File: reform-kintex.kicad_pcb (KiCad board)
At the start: 8 copper layers, 68 x 67.8 mm, 157 parts, among them J1 Conn_01x33, U1 MNT Reform 2.0 SoM Socket, U10 W25Q128JVS, U11 TPS62823DLC, U12 TPS62823DLC, U13 TPS62823DLC, U14 TPS62823DLC, U15 TPS62823DLC, U16 TPS62823DLC, U2 XC7K160T-FFG676, U3 IS43TR16512B-125KBLI, U4 IS43TR16512B-125KBLI, U5 TPS51200DRC, U6 KSZ9031RNXCA, U7 TUSB1310ZAY, U8 TC358778XBG, U9 SiI9022A

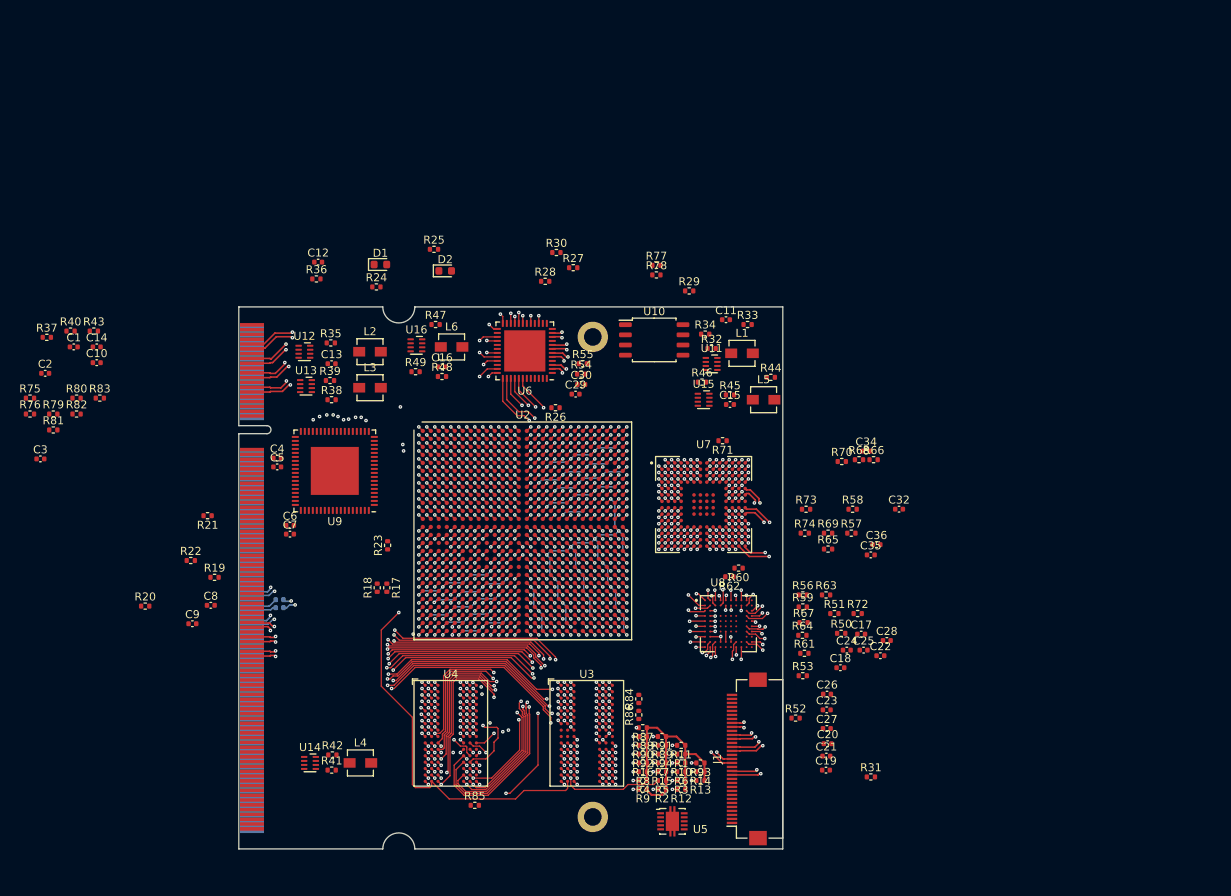
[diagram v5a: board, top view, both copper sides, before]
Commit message: more routing, bunch of fpga bypass caps, logo
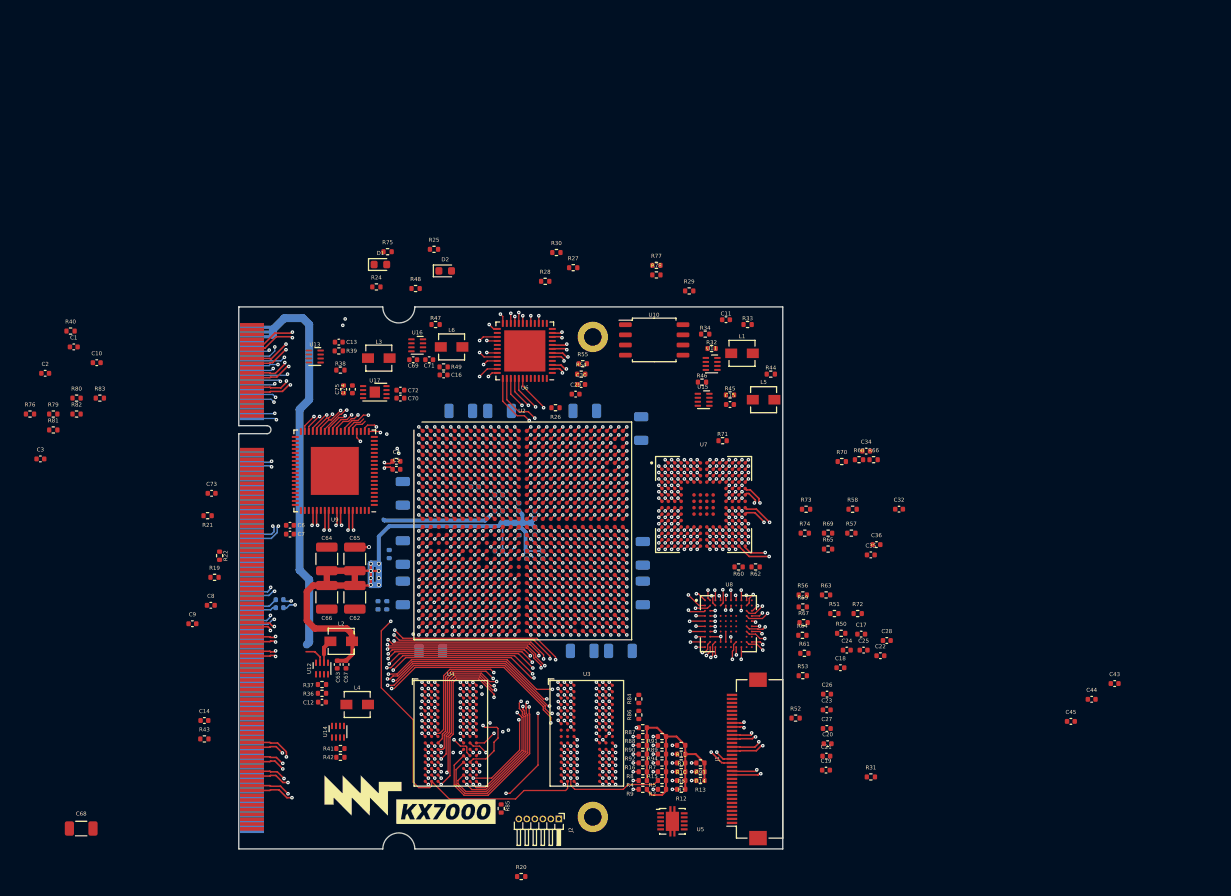
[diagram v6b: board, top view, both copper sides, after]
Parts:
- removed R35: R_Small, Resistor_SMD:R_0402_1005Metric
- added C37: 100uF, Capacitor_SMD:C_1206_3216Metric, B.Cu at (143.2, 113.0)
- added C38: 100uF, Capacitor_SMD:C_1206_3216Metric, B.Cu at (150.5, 135.8)
- added C39: 100uF, Capacitor_SMD:C_1206_3216Metric, B.Cu at (150.3, 115.2)
- added C40: 100uF, Capacitor_SMD:C_1206_3216Metric, B.Cu at (120.5, 123.3)
- added C41: 100uF, Capacitor_SMD:C_1206_3216Metric, B.Cu at (127.8, 113.0)
- added C42: 100uF, Capacitor_SMD:C_1206_3216Metric, B.Cu at (147.7, 143.0)
- added C43: 4.7uF, Capacitor_SMD:C_0402_1005Metric, F.Cu at (209.5, 147.1)
- added C44: 4.7uF, Capacitor_SMD:C_0402_1005Metric, F.Cu at (206.6, 149.1)
- added C45: 4.7uF, Capacitor_SMD:C_0402_1005Metric, F.Cu at (204.0, 151.8)
- added C46: 4.7uF, Capacitor_SMD:C_0402_1005Metric, B.Cu at (132.5, 125.5)
- added C47: 4.7uF, Capacitor_SMD:C_0402_1005Metric, B.Cu at (132.5, 123.5)
- added C48: 4.7uF, Capacitor_SMD:C_0402_1005Metric, B.Cu at (129.5, 122.5)
- added C49: 4.7uF, Capacitor_SMD:C_0402_1005Metric, B.Cu at (135.1, 128.1)
- added C50: 4.7uF, Capacitor_SMD:C_0402_1005Metric, B.Cu at (135.0, 125.0)
- added C51: 4.7uF, Capacitor_SMD:C_0402_1005Metric, B.Cu at (132.5, 130.5)
- added C52: 47uF, Capacitor_SMD:C_1206_3216Metric, B.Cu at (150.5, 130.8)
- added C53: 47uF, Capacitor_SMD:C_1206_3216Metric, B.Cu at (142.9, 143.0)
- added C54: 47uF, Capacitor_SMD:C_1206_3216Metric, B.Cu at (132.6, 113.0)
- added C55: 47uF, Capacitor_SMD:C_1206_3216Metric, B.Cu at (120.5, 130.7)
- added C56: 4.7uF, Capacitor_SMD:C_0402_1005Metric, B.Cu at (136.0, 131.0)
- added C57: 4.7uF, Capacitor_SMD:C_0402_1005Metric, B.Cu at (137.0, 128.0)
- added C58: 4.7uF, Capacitor_SMD:C_0402_1005Metric, B.Cu at (138.0, 131.0)
- added C59: 4.7uF, Capacitor_SMD:C_0402_1005Metric, B.Cu at (137.0, 126.0)
- added C60: 100uF, Capacitor_SMD:C_1206_3216Metric, B.Cu at (124.0, 143.0)
- added C61: 100uF, Capacitor_SMD:C_1206_3216Metric, B.Cu at (120.5, 135.8)
- added C62: 220uF, Capacitor_SMD:C_1210_3225Metric, F.Cu at (114.5, 136.3)
- added C63: 10uF, Capacitor_SMD:C_0402_1005Metric, F.Cu at (112.3, 144.7)
- added C64: 220uF, Capacitor_SMD:C_1210_3225Metric, F.Cu at (111.0, 131.5)
- added C65: 220uF, Capacitor_SMD:C_1210_3225Metric, F.Cu at (114.5, 131.5)
- added C66: 220uF, Capacitor_SMD:C_1210_3225Metric, F.Cu at (111.0, 136.3)
- added C67: 10uF, Capacitor_SMD:C_0402_1005Metric, F.Cu at (113.4, 144.7)
- added C68: 100uF, Capacitor_SMD:C_1206_3216Metric, F.Cu at (80.3, 165.2)
- added C69: 4.7uF, Capacitor_SMD:C_0402_1005Metric, F.Cu at (121.8, 106.6)
- added C70: 0.1uF, Capacitor_SMD:C_0402_1005Metric, F.Cu at (120.2, 111.4)
- added C71: 0.1uF, Capacitor_SMD:C_0402_1005Metric, F.Cu at (123.8, 106.6)
- added C72: 0.1uF, Capacitor_SMD:C_0402_1005Metric, F.Cu at (120.2, 110.4)
- added C73: 0.1uF, Capacitor_SMD:C_0402_1005Metric, F.Cu at (96.6, 123.3)
- added C74: 0.1uF, Capacitor_SMD:C_0402_1005Metric, F.Cu at (114.2, 110.3)
- added C75: 4.7uF, Capacitor_SMD:C_0402_1005Metric, F.Cu at (113.1, 110.3)
- added GFX1: MountingHole, footprints:mnt-kx7000, F.Cu at (121.4, 161.6)
- added J2: JTAG_01x06, Connector_PinHeader_1.00mm:PinHeader_1x06_P1.00mm_Horizontal, F.Cu at (140.0, 164.0)
- added U17: Si52112-B6, Package_DFN_QFN:TDFN-8-1EP_3x2mm_P0.5mm_EP1.3x1.4mm, F.Cu at (117.0, 110.7)
- R17, R18, R23: moved to B.Cu
- moved R20 57.9 mm to (135.3, 171.2)
- moved R37 55.4 mm to (110.4, 147.2)
- moved C12 55.0 mm to (110.4, 149.4), turned to 180 degrees
- moved R43 52.8 mm to (95.7, 154.0)
- moved R36 51.8 mm to (110.4, 148.3), turned to 180 degrees
- moved C14 48.6 mm to (95.7, 151.7)
- moved R75 48.3 mm to (118.6, 93.1)
- moved U12 39.7 mm to (110.4, 145.2), turned to 90 degrees
- moved L2 36.4 mm to (112.8, 141.8)
- moved C4 14.9 mm to (119.7, 119.3)
- moved C5 14.9 mm to (119.7, 120.3)
- moved R48 11.5 mm to (122.1, 97.7)
- moved L4 7.31 mm to (114.8, 149.7)
- moved U14 5.24 mm to (112.4, 153.1), turned to 90 degrees
- moved R39 3.86 mm to (112.5, 105.5)
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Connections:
- C12 pad 1: Net-(C12-Pad1) -> +1V0
- L2 pad 2: Net-(C12-Pad1) -> +1V0
- R36 pad 1: Net-(C12-Pad1) -> +1V0
- U12 pad 1: Net-(U12-Pad1) -> +5V
- U2 pad A8: DISP1_RGB6 -> DISP1_RGB5
- U2 pad A9: DISP1_RGB7 -> DISP1_RGB4
- U2 pad B9: DISP1_RGB4 -> DISP1_RGB6
- U2 pad C9: DISP1_RGB5 -> DISP1_RGB9
- U2 pad D10: DISP1_RGB0 -> DISP1_DE
- U2 pad D11: DISP1_VS -> DISP1_HS
- U2 pad D8: DISP1_RGB8 -> DISP1_RGB1
- U2 pad D9: DISP1_RGB9 -> DISP1_RGB10
- U2 pad E10: DISP1_RGB1 -> DISP1_RGB0
- U2 pad E11: DISP1_HS -> DISP1_VS
- U2 pad F10: DISP1_RGB2 -> DISP1_RGB7
- U2 pad F14: DISP1_DE -> DISP1_RGB11
- U2 pad F8: DISP1_RGB10 -> DISP1_RGB3
- U2 pad F9: DISP1_RGB11 -> DISP1_RGB2
- U2 pad G11: DISP1_RGB3 -> DISP1_RGB8
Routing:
- net +1V0: track 17.0 -> 106.6 mm, vias 24 -> 33
- net +5V: track 0.00 -> 57.7 mm
- net +1V8: track 93.3 -> 48.0 mm
- net HDMI_D2+: track 0.00 -> 44.6 mm, vias 0 -> 2
- net HDMI_D2-: track 0.00 -> 43.7 mm, vias 0 -> 2
- net SD2_DATA0: track 0.71 -> 43.2 mm, vias 1 -> 2
- net HDMI_D1+: track 0.00 -> 41.7 mm, vias 0 -> 2
- net HDMI_D1-: track 0.00 -> 40.9 mm, vias 0 -> 2
- net HDMI_D0+: track 0.00 -> 39.5 mm, vias 0 -> 2
- net HDMI_D0-: track 0.00 -> 38.6 mm, vias 0 -> 2
- net HDMI_CLK-: track 0.00 -> 37.9 mm, vias 0 -> 2
- net HDMI_CLK+: track 0.00 -> 36.3 mm, vias 0 -> 2
- net GND: track 161.3 -> 125.5 mm, vias 181 -> 182
- net SD2_CLK: track 0.71 -> 32.0 mm, vias 1 -> 2
- net SD2_DATA1: track 0.71 -> 29.1 mm, vias 1 -> 2
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
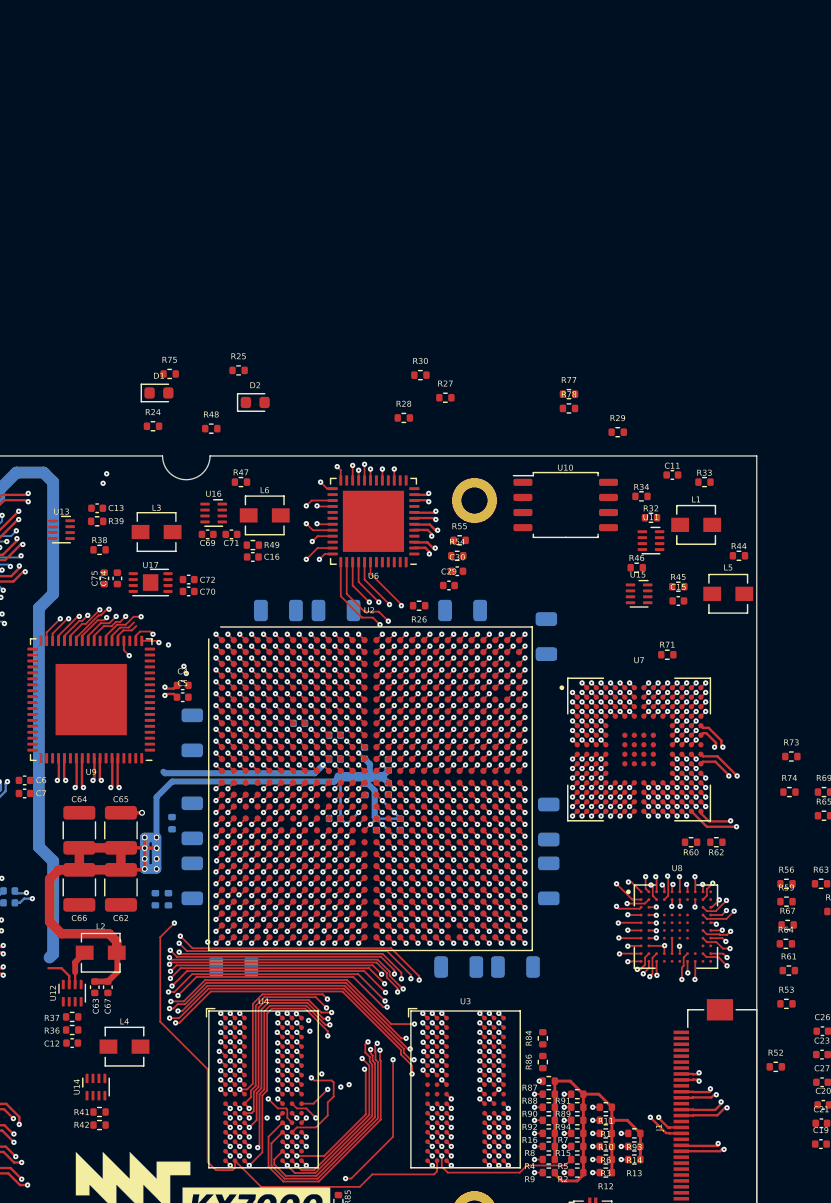
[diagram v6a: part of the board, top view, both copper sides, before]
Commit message: schematics: add many decoupling caps
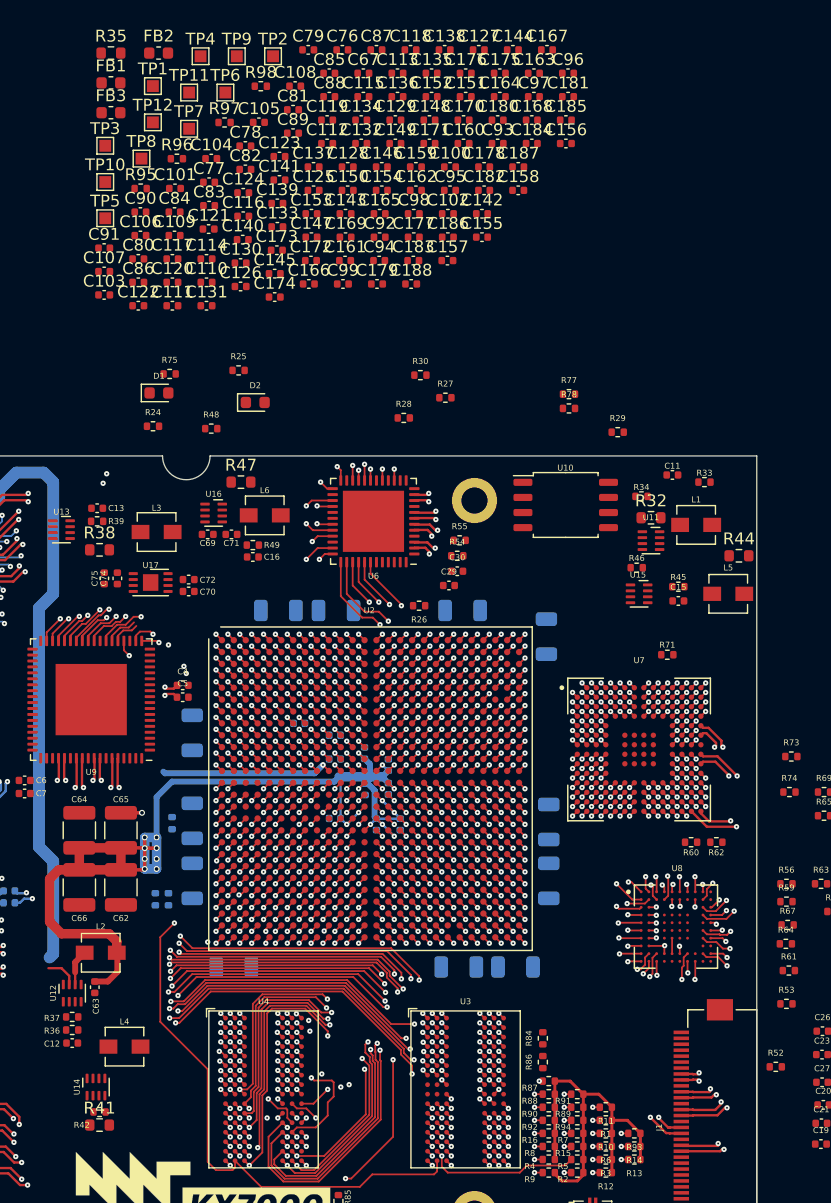
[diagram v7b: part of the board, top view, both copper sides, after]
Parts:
- added C100: 0.1uF, Capacitor_SMD:C_0402_1005Metric, F.Cu at (142.2, 75.7)
- added C101: 10uF, Capacitor_SMD:C_0402_1005Metric, F.Cu at (119.0, 77.5)
- added C102: 0.1uF, Capacitor_SMD:C_0402_1005Metric, F.Cu at (142.0, 79.6)
- added C103: 10nF, Capacitor_SMD:C_0402_1005Metric, F.Cu at (113.1, 86.5)
- added C104: 4.7uF, Capacitor_SMD:C_0402_1005Metric, F.Cu at (122.1, 75.0)
- added C105: 4.7uF, Capacitor_SMD:C_0402_1005Metric, F.Cu at (126.1, 71.9)
- added C106: 4.7uF, Capacitor_SMD:C_0402_1005Metric, F.Cu at (116.1, 81.5)
- added C107: 4.7uF, Capacitor_SMD:C_0402_1005Metric, F.Cu at (113.1, 84.5)
- added C108: 4.7uF, Capacitor_SMD:C_0402_1005Metric, F.Cu at (129.2, 68.9)
- added C109: 4.7uF, Capacitor_SMD:C_0402_1005Metric, F.Cu at (119.0, 81.5)
- added C110: 0.1uF, Capacitor_SMD:C_0402_1005Metric, F.Cu at (121.7, 85.4)
- added C111: 0.1uF, Capacitor_SMD:C_0402_1005Metric, F.Cu at (118.8, 87.4)
- added C112: 0.1uF, Capacitor_SMD:C_0402_1005Metric, F.Cu at (131.8, 73.7)
- added C113: 0.1uF, Capacitor_SMD:C_0402_1005Metric, F.Cu at (137.8, 67.8)
- added C114: 0.1uF, Capacitor_SMD:C_0402_1005Metric, F.Cu at (121.7, 83.4)
- added C115: 0.1uF, Capacitor_SMD:C_0402_1005Metric, F.Cu at (134.9, 69.8)
- added C116: 0.1uF, Capacitor_SMD:C_0402_1005Metric, F.Cu at (124.8, 79.8)
- added C117: 0.1uF, Capacitor_SMD:C_0402_1005Metric, F.Cu at (118.8, 83.4)
- added C118: 0.1uF, Capacitor_SMD:C_0402_1005Metric, F.Cu at (138.9, 65.8)
- added C119: 0.1uF, Capacitor_SMD:C_0402_1005Metric, F.Cu at (131.8, 71.7)
- added C120: 0.1uF, Capacitor_SMD:C_0402_1005Metric, F.Cu at (118.8, 85.4)
- added C121: 0.1uF, Capacitor_SMD:C_0402_1005Metric, F.Cu at (121.9, 80.9)
- added C122: 0.1uF, Capacitor_SMD:C_0402_1005Metric, F.Cu at (116.0, 87.4)
- added C123: 0.1uF, Capacitor_SMD:C_0402_1005Metric, F.Cu at (127.8, 74.8)
- added C124: 0.1uF, Capacitor_SMD:C_0402_1005Metric, F.Cu at (124.8, 77.9)
- added C125: 0.1uF, Capacitor_SMD:C_0402_1005Metric, F.Cu at (130.7, 77.7)
- added C126: 0.1uF, Capacitor_SMD:C_0402_1005Metric, F.Cu at (124.6, 85.7)
- added C127: 0.1uF, Capacitor_SMD:C_0402_1005Metric, F.Cu at (144.6, 65.8)
- added C128: 0.1uF, Capacitor_SMD:C_0402_1005Metric, F.Cu at (133.6, 75.7)
- added C129: 0.1uF, Capacitor_SMD:C_0402_1005Metric, F.Cu at (137.6, 71.7)
- added C130: 0.1uF, Capacitor_SMD:C_0402_1005Metric, F.Cu at (124.6, 83.8)
- added C131: 0.1uF, Capacitor_SMD:C_0402_1005Metric, F.Cu at (121.7, 87.4)
- added C132: 0.1uF, Capacitor_SMD:C_0402_1005Metric, F.Cu at (134.7, 73.7)
- added C133: 0.1uF, Capacitor_SMD:C_0402_1005Metric, F.Cu at (127.7, 80.7)
- added C134: 0.1uF, Capacitor_SMD:C_0402_1005Metric, F.Cu at (134.7, 71.7)
- added C135: 0.1uF, Capacitor_SMD:C_0402_1005Metric, F.Cu at (140.6, 67.8)
- added C136: 0.1uF, Capacitor_SMD:C_0402_1005Metric, F.Cu at (137.8, 69.8)
- added C137: 0.1uF, Capacitor_SMD:C_0402_1005Metric, F.Cu at (130.7, 75.7)
- added C138: 0.1uF, Capacitor_SMD:C_0402_1005Metric, F.Cu at (141.7, 65.8)
- added C139: 0.1uF, Capacitor_SMD:C_0402_1005Metric, F.Cu at (127.7, 78.8)
- added C140: 0.1uF, Capacitor_SMD:C_0402_1005Metric, F.Cu at (124.8, 81.8)
- added C141: 0.1uF, Capacitor_SMD:C_0402_1005Metric, F.Cu at (127.8, 76.8)
- added C142: 0.1uF, Capacitor_SMD:C_0402_1005Metric, F.Cu at (144.9, 79.6)
- added C143: 0.1uF, Capacitor_SMD:C_0402_1005Metric, F.Cu at (133.4, 79.6)
- added C144: 0.1uF, Capacitor_SMD:C_0402_1005Metric, F.Cu at (147.5, 65.8)
- added C145: 0.1uF, Capacitor_SMD:C_0402_1005Metric, F.Cu at (127.4, 84.7)
- added C146: 0.1uF, Capacitor_SMD:C_0402_1005Metric, F.Cu at (136.4, 75.7)
- added C147: 0.1uF, Capacitor_SMD:C_0402_1005Metric, F.Cu at (130.5, 81.6)
- added C148: 0.1uF, Capacitor_SMD:C_0402_1005Metric, F.Cu at (140.5, 71.7)
- added C149: 0.1uF, Capacitor_SMD:C_0402_1005Metric, F.Cu at (137.6, 73.7)
- added C150: 0.1uF, Capacitor_SMD:C_0402_1005Metric, F.Cu at (133.6, 77.7)
- added C151: 0.1uF, Capacitor_SMD:C_0402_1005Metric, F.Cu at (143.5, 69.8)
- added C152: 0.1uF, Capacitor_SMD:C_0402_1005Metric, F.Cu at (140.6, 69.8)
- added C153: 0.1uF, Capacitor_SMD:C_0402_1005Metric, F.Cu at (130.5, 79.6)
- added C154: 0.1uF, Capacitor_SMD:C_0402_1005Metric, F.Cu at (136.4, 77.7)
- added C155: 0.1uF, Capacitor_SMD:C_0402_1005Metric, F.Cu at (144.9, 81.6)
- added C156: 0.1uF, Capacitor_SMD:C_0402_1005Metric, F.Cu at (151.9, 73.7)
- added C157: 0.1uF, Capacitor_SMD:C_0402_1005Metric, F.Cu at (142.0, 83.6)
- added C158: 0.1uF, Capacitor_SMD:C_0402_1005Metric, F.Cu at (147.9, 77.7)
- added C159: 0.1uF, Capacitor_SMD:C_0402_1005Metric, F.Cu at (139.3, 75.7)
- added C160: 0.1uF, Capacitor_SMD:C_0402_1005Metric, F.Cu at (143.3, 73.7)
- added C161: 0.1uF, Capacitor_SMD:C_0402_1005Metric, F.Cu at (133.4, 83.6)
- added C162: 0.1uF, Capacitor_SMD:C_0402_1005Metric, F.Cu at (139.3, 77.7)
- added C163: 0.1uF, Capacitor_SMD:C_0402_1005Metric, F.Cu at (149.2, 67.8)
- added C164: 0.1uF, Capacitor_SMD:C_0402_1005Metric, F.Cu at (146.4, 69.8)
- added C165: 0.1uF, Capacitor_SMD:C_0402_1005Metric, F.Cu at (136.3, 79.6)
- added C166: 1uF, Capacitor_SMD:C_0402_1005Metric, F.Cu at (130.3, 85.5)
- added C167: 0.1uF, Capacitor_SMD:C_0402_1005Metric, F.Cu at (150.3, 65.8)
- added C168: 0.1uF, Capacitor_SMD:C_0402_1005Metric, F.Cu at (149.1, 71.7)
- added C169: 0.1uF, Capacitor_SMD:C_0402_1005Metric, F.Cu at (133.4, 81.6)
- added C170: 0.1uF, Capacitor_SMD:C_0402_1005Metric, F.Cu at (143.3, 71.7)
- added C171: 0.1uF, Capacitor_SMD:C_0402_1005Metric, F.Cu at (140.5, 73.7)
- added C172: 0.1uF, Capacitor_SMD:C_0402_1005Metric, F.Cu at (130.5, 83.6)
- added C173: 0.1uF, Capacitor_SMD:C_0402_1005Metric, F.Cu at (127.6, 82.7)
- added C174: 0.1uF, Capacitor_SMD:C_0402_1005Metric, F.Cu at (127.4, 86.6)
- added C175: 0.1uF, Capacitor_SMD:C_0402_1005Metric, F.Cu at (146.4, 67.8)
- added C176: 0.1uF, Capacitor_SMD:C_0402_1005Metric, F.Cu at (143.5, 67.8)
- added C177: 0.1uF, Capacitor_SMD:C_0402_1005Metric, F.Cu at (139.1, 81.6)
- added C178: 0.1uF, Capacitor_SMD:C_0402_1005Metric, F.Cu at (145.1, 75.7)
- added C179: 1uF, Capacitor_SMD:C_0402_1005Metric, F.Cu at (136.1, 85.5)
- added C180: 0.1uF, Capacitor_SMD:C_0402_1005Metric, F.Cu at (146.2, 71.7)
- added C181: 0.1uF, Capacitor_SMD:C_0402_1005Metric, F.Cu at (152.1, 69.8)
- added C182: 0.1uF, Capacitor_SMD:C_0402_1005Metric, F.Cu at (145.1, 77.7)
- added C183: 0.1uF, Capacitor_SMD:C_0402_1005Metric, F.Cu at (139.1, 83.6)
- added C184: 0.1uF, Capacitor_SMD:C_0402_1005Metric, F.Cu at (149.1, 73.7)
- added C185: 0.1uF, Capacitor_SMD:C_0402_1005Metric, F.Cu at (151.9, 71.7)
- added C186: 0.1uF, Capacitor_SMD:C_0402_1005Metric, F.Cu at (142.0, 81.6)
- added C187: 1uF, Capacitor_SMD:C_0402_1005Metric, F.Cu at (147.9, 75.7)
- added C188: 0.1uF, Capacitor_SMD:C_0402_1005Metric, F.Cu at (138.9, 85.5)
- added C76: 10uF, Capacitor_SMD:C_0402_1005Metric, F.Cu at (133.1, 65.8)
- added C77: 10uF, Capacitor_SMD:C_0402_1005Metric, F.Cu at (121.9, 77.0)
- added C78: 4.7uF, Capacitor_SMD:C_0402_1005Metric, F.Cu at (125.0, 73.9)
- added C79: 10uF, Capacitor_SMD:C_0402_1005Metric, F.Cu at (130.3, 65.8)
- added C80: 10uF, Capacitor_SMD:C_0402_1005Metric, F.Cu at (116.0, 83.4)
- added C81: 10uF, Capacitor_SMD:C_0402_1005Metric, F.Cu at (129.0, 70.9)
- added C82: 10uF, Capacitor_SMD:C_0402_1005Metric, F.Cu at (125.0, 75.9)
- added C83: 0.1uF, Capacitor_SMD:C_0402_1005Metric, F.Cu at (121.9, 78.9)
- added C84: 0.1uF, Capacitor_SMD:C_0402_1005Metric, F.Cu at (119.0, 79.5)
- added C85: 0.1uF, Capacitor_SMD:C_0402_1005Metric, F.Cu at (132.0, 67.8)
- added C86: 0.1uF, Capacitor_SMD:C_0402_1005Metric, F.Cu at (116.0, 85.4)
- added C87: 0.1uF, Capacitor_SMD:C_0402_1005Metric, F.Cu at (136.0, 65.8)
- added C88: 0.1uF, Capacitor_SMD:C_0402_1005Metric, F.Cu at (132.0, 69.8)
- added C89: 10uF, Capacitor_SMD:C_0402_1005Metric, F.Cu at (129.0, 72.8)
- added C90: 0.1uF, Capacitor_SMD:C_0402_1005Metric, F.Cu at (116.1, 79.5)
- added C91: 0.1uF, Capacitor_SMD:C_0402_1005Metric, F.Cu at (113.1, 82.5)
- added C92: 0.1uF, Capacitor_SMD:C_0402_1005Metric, F.Cu at (136.3, 81.6)
- added C93: 10uF, Capacitor_SMD:C_0402_1005Metric, F.Cu at (146.2, 73.7)
- added C94: 10uF, Capacitor_SMD:C_0402_1005Metric, F.Cu at (136.2, 83.6)
- added C95: 0.1uF, Capacitor_SMD:C_0402_1005Metric, F.Cu at (142.2, 77.7)
- added C96: 0.1uF, Capacitor_SMD:C_0402_1005Metric, F.Cu at (152.1, 67.8)
- added C97: 10uF, Capacitor_SMD:C_0402_1005Metric, F.Cu at (149.2, 69.8)
- added C98: 10uF, Capacitor_SMD:C_0402_1005Metric, F.Cu at (139.1, 79.6)
- added C99: 0.1uF, Capacitor_SMD:C_0402_1005Metric, F.Cu at (133.2, 85.5)
- added FB1: Ferrite_Bead_Small, Inductor_SMD:L_0603_1608Metric, F.Cu at (113.7, 68.6)
- added FB2: Ferrite_Bead_Small, Inductor_SMD:L_0603_1608Metric, F.Cu at (117.7, 66.1)
- added FB3: Ferrite_Bead_Small, Inductor_SMD:L_0603_1608Metric, F.Cu at (113.7, 71.1)
- added R35: 0, Resistor_SMD:R_0603_1608Metric, F.Cu at (113.7, 66.1)
- added R95: 4.7k, Resistor_SMD:R_0402_1005Metric, F.Cu at (116.2, 77.5)
- added R96: 5.1k, Resistor_SMD:R_0402_1005Metric, F.Cu at (119.2, 75.0)
- added R97: 10k, Resistor_SMD:R_0402_1005Metric, F.Cu at (123.2, 71.9)
- added R98: 100, Resistor_SMD:R_0402_1005Metric, F.Cu at (126.3, 68.9)
- added TP1: TestPoint, TestPoint:TestPoint_Pad_1.0x1.0mm, F.Cu at (117.2, 68.9)
- added TP10: TUSBJ_TDI, TestPoint:TestPoint_Pad_1.0x1.0mm, F.Cu at (113.2, 77.0)
- added TP11: TUSBJ_TRSTN, TestPoint:TestPoint_Pad_1.0x1.0mm, F.Cu at (120.2, 69.4)
- added TP12: TUSBJ_TDO, TestPoint:TestPoint_Pad_1.0x1.0mm, F.Cu at (117.2, 71.9)
- added TP2: TestPoint, TestPoint:TestPoint_Pad_1.0x1.0mm, F.Cu at (127.3, 66.4)
- added TP3: TestPoint, TestPoint:TestPoint_Pad_1.0x1.0mm, F.Cu at (113.2, 73.9)
- added TP4: TestPoint, TestPoint:TestPoint_Pad_1.0x1.0mm, F.Cu at (121.2, 66.4)
- added TP5: TestPoint, TestPoint:TestPoint_Pad_1.0x1.0mm, F.Cu at (113.2, 80.0)
- added TP6: TestPoint, TestPoint:TestPoint_Pad_1.0x1.0mm, F.Cu at (123.3, 69.4)
- added TP7: TestPoint, TestPoint:TestPoint_Pad_1.0x1.0mm, F.Cu at (120.2, 72.5)
- added TP8: TUSBJ_TCK, TestPoint:TestPoint_Pad_1.0x1.0mm, F.Cu at (116.2, 75.0)
- added TP9: TUSBJ_TMS, TestPoint:TestPoint_Pad_1.0x1.0mm, F.Cu at (124.2, 66.4)
- C67: value 10uF -> 4.7uF
- R32, R38, R41, R44, R47: value R_Small -> 0; footprint Resistor_SMD:R_0402_1005Metric -> Resistor_SMD:R_0603_1608Metric
- moved C67 79.8 mm to (134.9, 67.8), turned to 0 degrees
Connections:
- net Net-(U9-Pad1) renamed DISP1_SCL
- net Net-(U9-Pad2) renamed DISP1_SDA
- C12 pad 1: +1V0 -> Net-(C12-Pad1)
- C63 pad 1: +1V0 -> Net-(C12-Pad1)
- C67 pad 1: +1V0 -> GND
- C67 pad 2: GND -> +5V
- L2 pad 2: +1V0 -> Net-(C12-Pad1)
- R36 pad 1: +1V0 -> Net-(C12-Pad1)
- U12 pad 1: +5V -> Net-(U12-Pad1)
- U2 pad M5: Net-(U2-PadM5) -> +1V2
- U6 pad 1: Net-(U6-Pad1) -> ETH_VDDA
- U6 pad 12: Net-(U6-Pad12) -> ETH_VDDA
- U6 pad 4: Net-(U6-Pad4) -> ETH_VDDL
- U6 pad 44: Net-(U6-Pad44) -> ETH_VDDL_PLL
- U6 pad 9: Net-(U6-Pad9) -> ETH_VDDL
- U9 pad 21: Net-(U9-Pad21) -> +1V8
- U9 pad 3: Net-(U9-Pad3) -> +1V8
- U9 pad 43: Net-(U9-Pad43) -> GND
- U9 pad 46: Net-(U9-Pad46) -> +1V8
- U9 pad 48: Net-(U9-Pad48) -> HDMI_SDA
- U9 pad 49: Net-(U9-Pad49) -> HDMI_SCL
- U9 pad 50: Net-(U9-Pad50) -> HDMI_CEC
- U9 pad 54: Net-(U9-Pad54) -> HDMI_HPD
- U9 pad 55: Net-(U9-Pad55) -> GND
- U9 pad 60: Net-(U9-Pad60) -> +1V2
- U9 pad 69: Net-(U9-Pad69) -> GND
- U9 pad 70: Net-(U9-Pad70) -> GND
- U9 pad 73: Net-(U9-Pad73) -> GND
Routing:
- net +1V2: track 12.7 -> 13.4 mm, vias 11 -> 12
- net Net-(U2-PadM5): track 0.71 -> 0.00 mm, vias 1 -> 0

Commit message: ram bypass caps placed
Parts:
- C130, C131, C132, C133, C134, C135, C136, C137, C138, C139, C140, C141, C142, C143, C144, C145, C146, C147, C148, C149, C150, C151, C152, C153, C154, C155, C156, C157, C158, C159, C160, C161, C162, C163, C164, C165: moved to B.Cu
- moved C156 90.3 mm to (122.2, 159.0), turned to 180 degrees
- moved C163 88.7 mm to (131.5, 154.8)
- moved C164 88.7 mm to (131.5, 157.2)
- moved C138 86.9 mm to (147.8, 152.5)
- moved C144 86.3 mm to (143.0, 152.0)
- moved C132 85.8 mm to (143.8, 159.0), turned to 180 degrees
- moved C152 82.5 mm to (126.0, 151.0)
- moved C151 82.1 mm to (126.0, 150.0)
- moved C135 81.0 mm to (147.8, 148.5)
- moved C136 80.4 mm to (147.8, 149.5)
- moved C165 79.5 mm to (131.5, 159.0)
- moved C146 79.4 mm to (139.2, 155.0), turned to 180 degrees
- moved C133 79.1 mm to (139.2, 159.0), turned to 180 degrees
- moved C155 79.0 mm to (122.2, 157.2), turned to 180 degrees
- moved C154 78.6 mm to (122.2, 155.0), turned to 180 degrees
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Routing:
- net +1V5: track 30.5 -> 171.2 mm, vias 46 -> 48
- net GND: track 125.5 -> 164.4 mm, vias 182 -> 186
- net RAM_RAS#: track 86.8 -> 70.4 mm
- net Net-(R84-Pad1): track 0.57 -> 8.58 mm
- net RAM_CK+: track 53.7 -> 55.1 mm, vias 3 -> 4
- net RAM_CK-: track 56.1 -> 57.3 mm, vias 3 -> 4
- net RAM_BA1: track 56.0 -> 54.9 mm
- net RAM_A5: track 61.4 -> 62.4 mm
- net VTTREF: track 17.0 -> 17.6 mm, vias 7 -> 8
- added copper zone on B.Cu, net GND
